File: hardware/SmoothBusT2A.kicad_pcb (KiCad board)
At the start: 2 copper layers, 28.2 x 29 mm, 6 parts, among them U1 ATTINY85-20SU, U2 MC7805BDTRKG

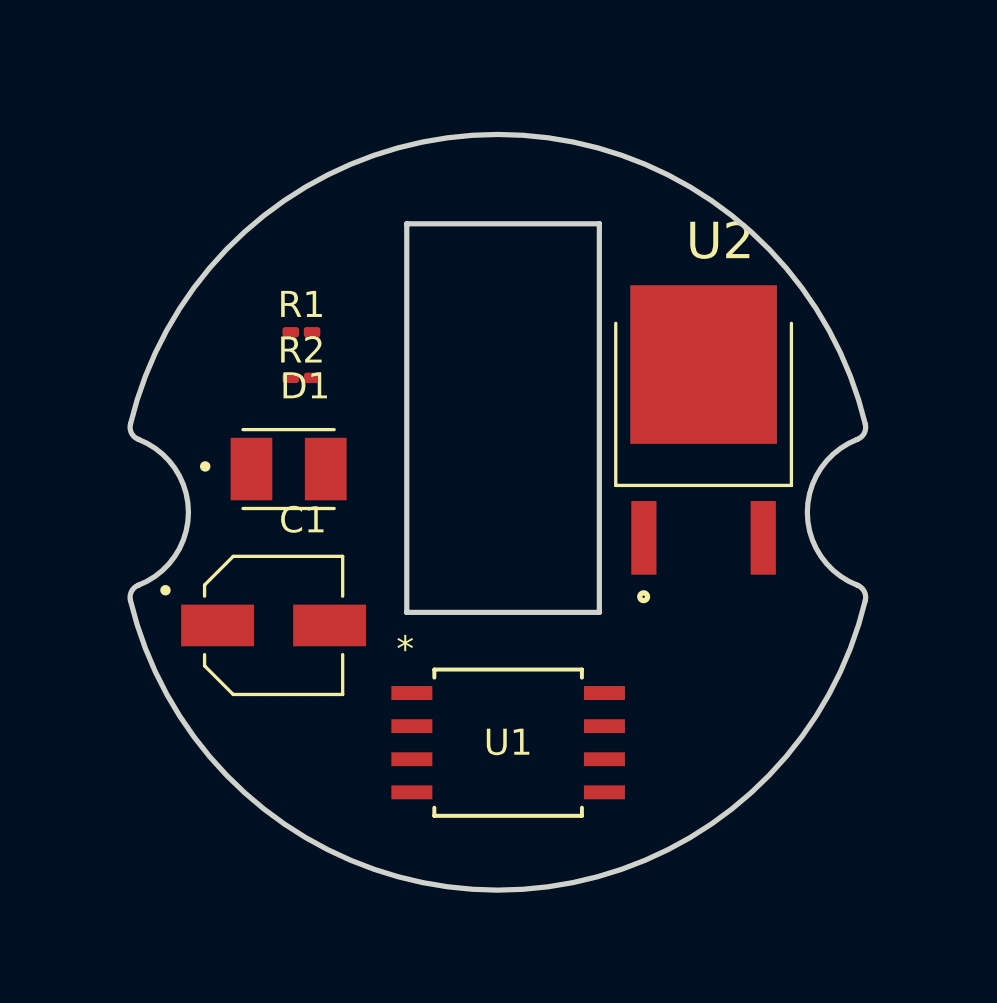
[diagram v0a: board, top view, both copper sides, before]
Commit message: added parts to pcb
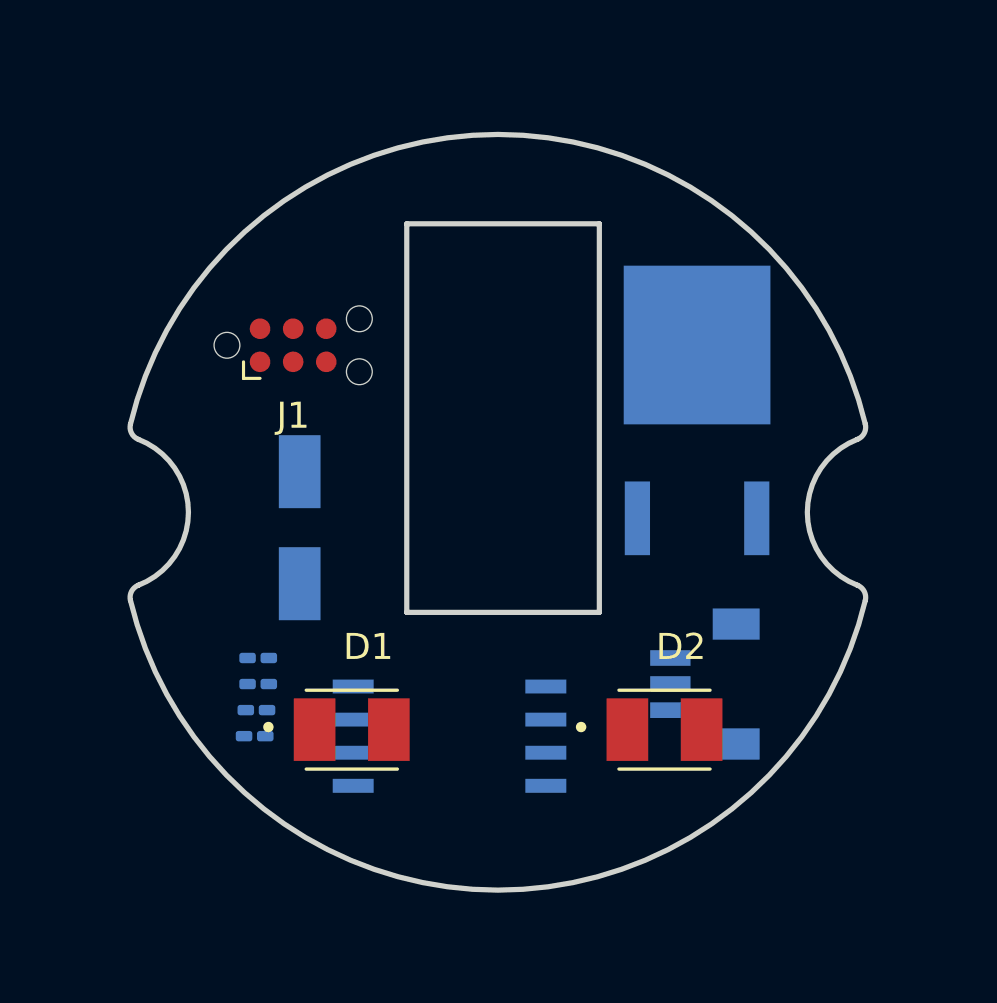
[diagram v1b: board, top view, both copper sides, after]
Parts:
- added D2: OF-SMD3528WC, OF-SMD3528WC:LED_OF-SMD3528WC, F.Cu at (75.0, 66.5)
- added J1: Conn_ARM_SWD_TagConnect_TC2030-NL, Connector:Tag-Connect_TC2030-IDC-NL_2x03_P1.27mm_Vertical, F.Cu at (60.8, 51.8)
- added J2: BM03B-SRSS-TB_LF__SN_, BM03B-SRSS-TB_LF__SN_:JST_BM03B-SRSS-TB_LF__SN_, B.Cu at (77.8, 64.8)
- added R3: R300, Resistor_SMD:R_0201_0603Metric_Pad0.64x0.40mm_HandSolder, B.Cu at (59.3, 65.8)
- added R4: R300, Resistor_SMD:R_0201_0603Metric_Pad0.64x0.40mm_HandSolder, B.Cu at (59.3, 66.8)
- C1, R1, R2, U1, U2: moved to B.Cu
- moved R1 12.6 mm to (59.4, 63.8), turned to 180 degrees
- moved R2 11.9 mm to (59.4, 64.8), turned to 180 degrees
- moved D1 10.3 mm to (63.0, 66.5)
- moved C1 3.88 mm to (61.0, 58.8), turned to -90 degrees
- moved U1 2.26 mm to (66.8, 66.8), turned to 180 degrees
- moved U2 0.79 mm to (76.2, 54.2), turned to 180 degrees
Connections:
- C1 pad 1: unconnected-(C1-Pad1) -> 5V
- C1 pad 2: unconnected-(C1-Pad2) -> GND
- D1 pad 1: unconnected-(D1-Pad1) -> Net-(D1-Pad1)
- D1 pad 2: unconnected-(D1-Pad2) -> GND
- R1 pad 1: unconnected-(R1-Pad1) -> 5V
- R1 pad 2: unconnected-(R1-Pad2) -> Probe_PB2
- R2 pad 1: unconnected-(R2-Pad1) -> LED_Out
- R2 pad 2: unconnected-(R2-Pad2) -> Net-(D1-Pad1)
- U1 pad 1: unconnected-(U1-(PCINT5/RESET*/ADC0/dW)_PB5-Pad1) -> Probe_PB5
- U1 pad 2: unconnected-(U1-(PCINT3/XTAL1/CLKI/OC1B*/ADC3)_PB3-Pad2) -> Probe_PB3
- U1 pad 3: unconnected-(U1-(PCINT4/XTAL2/CLKO/OC1B/ADC2)_PB4-Pad3) -> Probe_PB4
- U1 pad 4: unconnected-(U1-GND-Pad4) -> GND
- U1 pad 5: unconnected-(U1-PB0_(MOSI/DI/SDA/AIN0/OC0A/OC1A/AREF/PCINT0)-Pad5) -> Probe_PB0
- U1 pad 6: unconnected-(U1-PB1_(MISO/DO/AIN1/OC0B/OC1A*/PCINT1)-Pad6) -> LED_Out
- U1 pad 7: unconnected-(U1-PB2_(SCK/USCK/SCL/ADC1/T0/INT0/PCINT2)-Pad7) -> Probe_PB2
- U1 pad 8: unconnected-(U1-VCC-Pad8) -> 5V

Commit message: routing traces
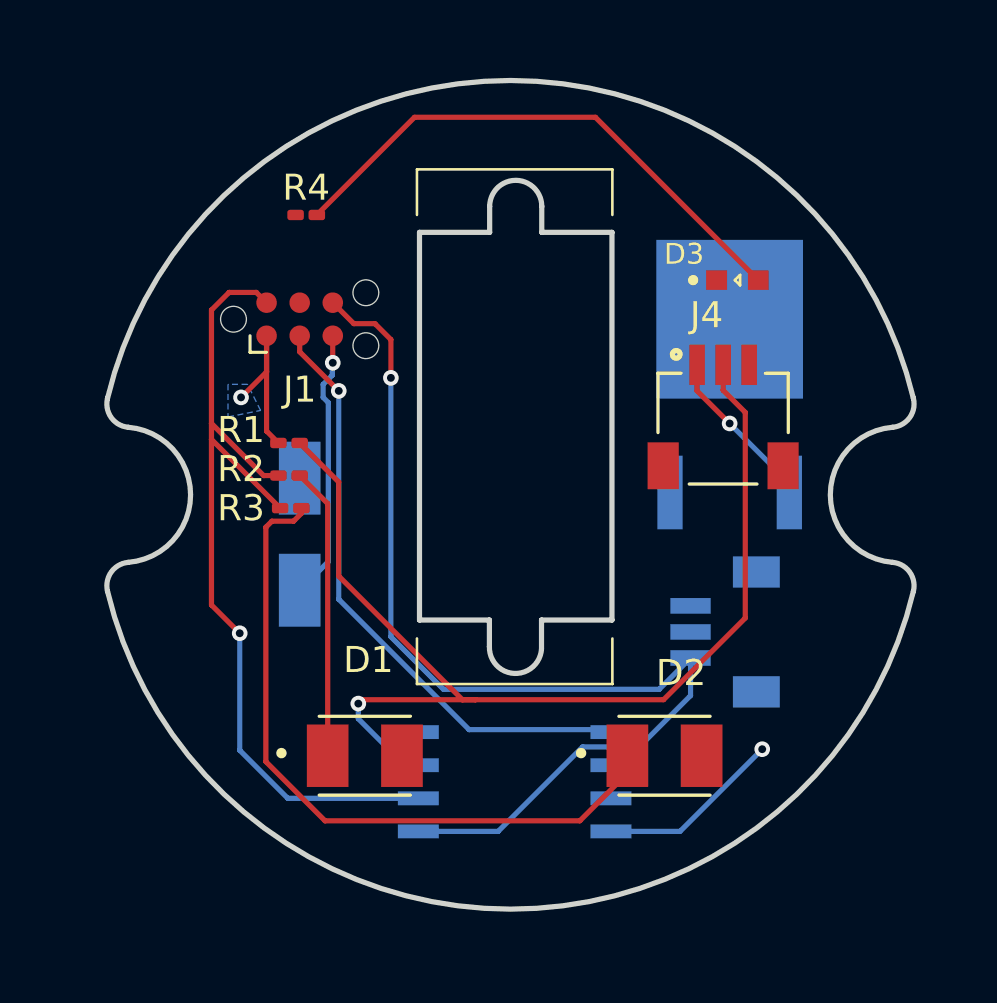
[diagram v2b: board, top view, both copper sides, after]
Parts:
- added D3: WL-SMCD_0603, 150060VS55040:WL-SMCD_0603, F.Cu at (77.8, 49.2)
- added J4: SM03B-SRSS-TB_LF__SN_, SM03B_SRSS_TB_LF__SN_:JST_SM03B-SRSS-TB_LF__SN_, F.Cu at (77.2, 52.5)
- D1: value OF-SMD3528WC -> Attiny85
- R1, R2, R3, R4: moved to F.Cu
- moved R4 20.1 mm to (61.2, 46.8), turned to 0 degrees
- moved R1 8.33 mm to (60.6, 55.5), turned to 0 degrees
- moved R2 8.09 mm to (60.6, 56.8), turned to 0 degrees
- moved R3 7.86 mm to (60.7, 58.0), turned to 0 degrees
- moved U1 3.05 mm to (69.2, 68.5)
- moved J2 2.14 mm to (78.5, 62.8)
- moved U2 1.59 mm to (77.5, 53.3)
- moved D1 1.12 mm to (63.5, 67.5)
- moved J1 1.03 mm to (61.0, 50.8)
- moved D2 1.00 mm to (75.0, 67.5)
- moved C1 0.25 mm to (61.0, 59.0)
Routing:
- net Probe_PB2: track 0.00 -> 42.8 mm, vias 0 -> 1
- net Probe_PB0: track 0.00 -> 40.7 mm, vias 0 -> 1
- net LED_Out: track 0.00 -> 34.6 mm, vias 0 -> 1
- net Net-(D2-Pad1): track 0.00 -> 27.0 mm
- net Probe_PB5: track 0.00 -> 22.8 mm, vias 0 -> 1
- net Net-(D3-Pad2): track 0.00 -> 21.1 mm
- net GND: track 0.14 -> 17.5 mm, vias 0 -> 2
- net Net-(D1-Pad1): track 0.00 -> 11.2 mm
- net 5V: track 0.00 -> 7.07 mm, vias 0 -> 1
- net 12V: track 0.00 -> 6.37 mm, vias 0 -> 1
- added copper zone on B.Cu, net 5V
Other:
- board size 28.2 x 29 mm -> 31 x 31.8 mm

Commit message: finish tracing and add bom
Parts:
- D1: value Attiny85 -> OF-SMD3528WC
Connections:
- J1 pad 4: unconnected-(J1-SWCLK-Pad4) -> Probe_PB2
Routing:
- net 5V: track 7.07 -> 73.2 mm, vias 1 -> 6
- net GND: track 17.5 -> 40.0 mm, vias 2 -> 6
- net Probe_PB2: track 42.8 -> 59.5 mm, vias 1 -> 3
- net Probe_PB0: track 40.7 -> 45.0 mm
- added copper zone on F.Cu, net 5V
- added copper zone on B.Cu, net GND
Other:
- board text added: "Designed in Berlin"
- board text added: "Smoothbus T2A"

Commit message: version 1
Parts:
- added R5: R10k, 150060VS55040:WL-SMCD_0603, B.Cu at (75.5, 67.8)
- added R6: R10k, 150060VS55040:WL-SMCD_0603, B.Cu at (75.5, 69.2)
- R1, R2, R3, R4: footprint Resistor_SMD:R_0201_0603Metric_Pad0.64x0.40mm_HandSolder -> 150060VS55040:WL-SMCD_0603
- moved R1 0.29 mm to (60.3, 55.5)
- moved R2 0.29 mm to (60.3, 56.8)
- moved R3 0.29 mm to (60.4, 58.0)
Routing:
- net GND: track 40.0 -> 33.3 mm
- net LED_Out: track 34.6 -> 40.7 mm
- net Probe_PB0: track 45.0 -> 48.1 mm
- net Probe_PB4: track 0.00 -> 1.96 mm
- net Probe_PB3: track 0.00 -> 1.80 mm
- net Probe_PB2: track 59.5 -> 58.7 mm
- net 5V: track 73.2 -> 73.8 mm, vias 6 -> 8
- removed copper zone on B.Cu, net 5V
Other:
- board text added: "Heath Lee"
- board text added: "PWR Fuel Sender"
- board text added: "Servo"
- board text removed: "Designed in Berlin"
